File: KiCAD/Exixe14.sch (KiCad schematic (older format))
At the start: 18 parts, among them U4 EXIXE14, U5 EXIXE14, U6 EXIXE14, U7 EXIXE14, U8 EXIXE14, U9 EXIXE14

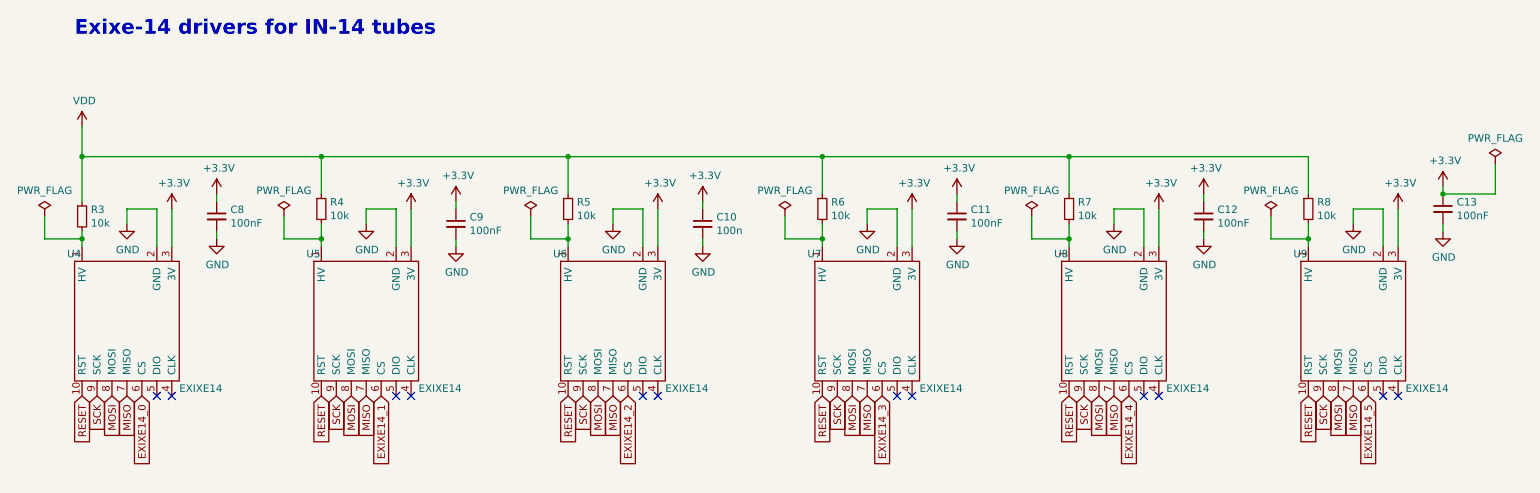
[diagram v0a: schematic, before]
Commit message: v01.2: Updated component numbers, title block, and added transistor library.
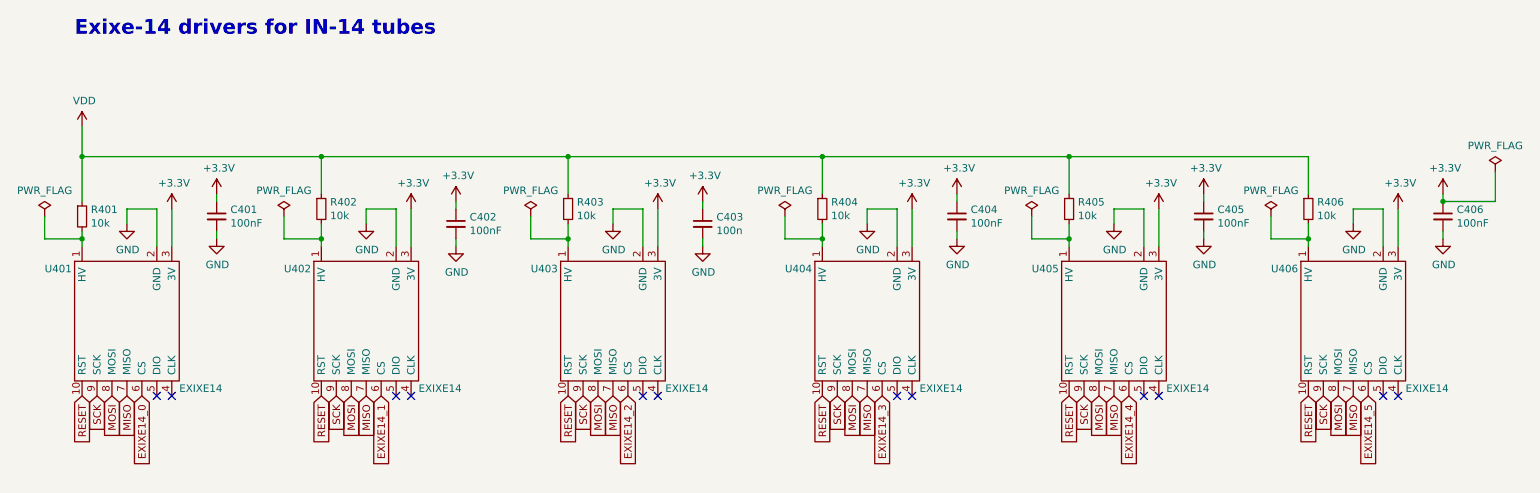
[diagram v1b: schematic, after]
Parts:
- renumbered C8 to C401, C9 to C402, C10 to C403, C11 to C404, C12 to C405, C13 to C406, R3 to R401, R4 to R402, R5 to R403, R6 to R404, R7 to R405, R8 to R406, U4 to U401, U5 to U402, U6 to U403, U7 to U404, U8 to U405, U9 to U406
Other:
- moved on the sheet: C406
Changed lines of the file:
@@
 Sheet 4 5
 Title "Nixie Tube Clock Host Board"
-Date "2021-04-20"
-Rev "v01.1"
+Date "2021-04-26"
+Rev "v01.2"
 Comp "University of Alberta (AlbertaSat)"
-Comment1 "License: CC BY 4.0 (https://creativecommons.org/licenses/by/4.0/)"
-Comment2 "Steven Knudsen (ECE dept., Faculty of Engineering, University of Alberta)."
-Comment3 "This schematic was designed with the assistance of "
-Comment4 "Author: Pundeep Hundal                   Co-author: Sichun Xu"
+Comment1 ""
+Comment2 "License: CC BY 4.0 (https://creativecommons.org/licenses/by/4.0/)"
+Comment3 "Co-author: Sichun Xu"
+Comment4 "Author: Pundeep Hundal"
 $EndDescr
 $Comp
@@
 P 1800 3600
 AR Path="/60980F67" Ref="U?"  Part="1"
-AR Path="/6091CAEB/60980F67" Ref="U4"  Part="1"
-F 0 "U4" H 1400 4050 50  0000 L CNN
+AR Path="/6091CAEB/60980F67" Ref="U401"  Part="1"
+F 0 "U401" H 1250 3950 50  0000 L CNN
 F 1 "EXIXE14" H 2150 3150 50  0000 L CNN
 F 2 "" H 1800 3300 50  0001 C CNN
@@
 P 3400 3600
 AR Path="/60980F6D" Ref="U?"  Part="1"
-AR Path="/6091CAEB/60980F6D" Ref="U5"  Part="1"
-F 0 "U5" H 3000 4050 50  0000 L CNN
+AR Path="/6091CAEB/60980F6D" Ref="U402"  Part="1"
+F 0 "U402" H 2850 3950 50  0000 L CNN
 F 1 "EXIXE14" H 3750 3150 50  0000 L CNN
 F 2 "" H 3400 3300 50  0001 C CNN
@@
 P 5050 3600
 AR Path="/60980F73" Ref="U?"  Part="1"
-AR Path="/6091CAEB/60980F73" Ref="U6"  Part="1"
-F 0 "U6" H 4650 4050 50  0000 L CNN
+AR Path="/6091CAEB/60980F73" Ref="U403"  Part="1"
+F 0 "U403" H 4500 3950 50  0000 L CNN
 F 1 "EXIXE14" H 5400 3150 50  0000 L CNN
 F 2 "" H 5050 3300 50  0001 C CNN
@@
 P 6750 3600
 AR Path="/60980F79" Ref="U?"  Part="1"
-AR Path="/6091CAEB/60980F79" Ref="U7"  Part="1"
-F 0 "U7" H 6350 4050 50  0000 L CNN
+AR Path="/6091CAEB/60980F79" Ref="U404"  Part="1"
+F 0 "U404" H 6200 3950 50  0000 L CNN
 F 1 "EXIXE14" H 7100 3150 50  0000 L CNN
 F 2 "" H 6750 3300 50  0001 C CNN
@@
 P 8400 3600
 AR Path="/60980F7F" Ref="U?"  Part="1"
-AR Path="/6091CAEB/60980F7F" Ref="U8"  Part="1"
-F 0 "U8" H 8000 4050 50  0000 L CNN
+AR Path="/6091CAEB/60980F7F" Ref="U405"  Part="1"
+F 0 "U405" H 7850 3950 50  0000 L CNN
 F 1 "EXIXE14" H 8750 3150 50  0000 L CNN
 F 2 "" H 8400 3300 50  0001 C CNN
@@
 P 10000 3600
 AR Path="/60980F85" Ref="U?"  Part="1"
-AR Path="/6091CAEB/60980F85" Ref="U9"  Part="1"
-F 0 "U9" H 9600 4050 50  0000 L CNN
+AR Path="/6091CAEB/60980F85" Ref="U406"  Part="1"
+F 0 "U406" H 9450 3950 50  0000 L CNN
 F 1 "EXIXE14" H 10350 3150 50  0000 L CNN
 F 2 "" H 10000 3300 50  0001 C CNN
@@
 P 2400 2900
 AR Path="/60981009" Ref="C?"  Part="1"
-AR Path="/6091CAEB/60981009" Ref="C8"  Part="1"
-F 0 "C8" H 2492 2946 50  0000 L CNN
+AR Path="/6091CAEB/60981009" Ref="C401"  Part="1"
+F 0 "C401" H 2492 2946 50  0000 L CNN
 F 1 "100nF" H 2492 2855 50  0000 L CNN
 F 2 "" H 2400 2900 50  0001 C CNN
@@
 P 4000 2950
 AR Path="/60981017" Ref="C?"  Part="1"
-AR Path="/6091CAEB/60981017" Ref="C9"  Part="1"
-F 0 "C9" H 4092 2996 50  0000 L CNN
+AR Path="/6091CAEB/60981017" Ref="C402"  Part="1"
+F 0 "C402" H 4092 2996 50  0000 L CNN
 F 1 "100nF" H 4092 2905 50  0000 L CNN
 F 2 "" H 4000 2950 50  0001 C CNN
@@
 P 5650 2950
 AR Path="/6098101D" Ref="C?"  Part="1"
-AR Path="/6091CAEB/6098101D" Ref="C10"  Part="1"
-F 0 "C10" H 5742 2996 50  0000 L CNN
+AR Path="/6091CAEB/6098101D" Ref="C403"  Part="1"
+F 0 "C403" H 5742 2996 50  0000 L CNN
 F 1 "100n" H 5742 2905 50  0000 L CNN
 F 2 "" H 5650 2950 50  0001 C CNN
@@
 P 7350 2900
 AR Path="/60981023" Ref="C?"  Part="1"
-AR Path="/6091CAEB/60981023" Ref="C11"  Part="1"
-F 0 "C11" H 7442 2946 50  0000 L CNN
+AR Path="/6091CAEB/60981023" Ref="C404"  Part="1"
+F 0 "C404" H 7442 2946 50  0000 L CNN
 F 1 "100nF" H 7442 2855 50  0000 L CNN
 F 2 "" H 7350 2900 50  0001 C CNN
@@
 P 9000 2900
 AR Path="/60981029" Ref="C?"  Part="1"
-AR Path="/6091CAEB/60981029" Ref="C12"  Part="1"
-F 0 "C12" H 9092 2946 50  0000 L CNN
+AR Path="/6091CAEB/60981029" Ref="C405"  Part="1"
+F 0 "C405" H 9092 2946 50  0000 L CNN
 F 1 "100nF" H 9092 2855 50  0000 L CNN
 F 2 "" H 9000 2900 50  0001 C CNN
@@
 L Device:C_Small C?
 U 1 1 6098102F
-P 10600 2850
+P 10600 2900
 AR Path="/6098102F" Ref="C?"  Part="1"
-AR Path="/6091CAEB/6098102F" Ref="C13"  Part="1"
-F 0 "C13" H 10692 2896 50  0000 L CNN
-F 1 "100nF" H 10692 2805 50  0000 L CNN
-F 2 "" H 10600 2850 50  0001 C CNN
-F 3 "~" H 10600 2850 50  0001 C CNN
-	1    10600 2850
+AR Path="/6091CAEB/6098102F" Ref="C406"  Part="1"
+F 0 "C406" H 10692 2946 50  0000 L CNN
+F 1 "100nF" H 10692 2855 50  0000 L CNN
+F 2 "" H 10600 2900 50  0001 C CNN
+F 3 "~" H 10600 2900 50  0001 C CNN
+	1    10600 2900
 	1    0    0    -1
 $EndComp
@@
 L power:+3.3V #PWR?
 U 1 1 6098106D
-P 10600 2700
+P 10600 2750
 AR Path="/6098106D" Ref="#PWR?"  Part="1"
 AR Path="/6091CAEB/6098106D" Ref="#PWR048"  Part="1"
-F 0 "#PWR048" H 10600 2550 50  0001 C CNN
-F 1 "+3.3V" H 10615 2873 50  0000 C CNN
-F 2 "" H 10600 2700 50  0001 C CNN
-F 3 "" H 10600 2700 50  0001 C CNN
-	1    10600 2700
-	1    0    0    -1
-$EndComp
-Wire Wire Line
-	10600 2700 10600 2750
+F 0 "#PWR048" H 10600 2600 50  0001 C CNN
+F 1 "+3.3V" H 10615 2923 50  0000 C CNN
+F 2 "" H 10600 2750 50  0001 C CNN
+F 3 "" H 10600 2750 50  0001 C CNN
+	1    10600 2750
+	1    0    0    -1
+$EndComp
+Wire Wire Line
+	10600 2750 10600 2800
 $Comp
 L power:GND #PWR?
 U 1 1 60981074
-P 10600 3000
+P 10600 3050
 AR Path="/60981074" Ref="#PWR?"  Part="1"
 AR Path="/6091CAEB/60981074" Ref="#PWR049"  Part="1"
-F 0 "#PWR049" H 10600 2750 50  0001 C CNN
-F 1 "GND" H 10605 2827 50  0000 C CNN
-F 2 "" H 10600 3000 50  0001 C CNN
-F 3 "" H 10600 3000 50  0001 C CNN
-	1    10600 3000
-	1    0    0    -1
-$EndComp
-Wire Wire Line
-	10600 3000 10600 2950
+F 0 "#PWR049" H 10600 2800 50  0001 C CNN
+F 1 "GND" H 10605 2877 50  0000 C CNN
+F 2 "" H 10600 3050 50  0001 C CNN
+F 3 "" H 10600 3050 50  0001 C CNN
+	1    10600 3050
+	1    0    0    -1
+$EndComp
+Wire Wire Line
+	10600 3050 10600 3000
 $Comp
 L Device:R_Small R?
@@
 P 3100 2850
 AR Path="/6098107B" Ref="R?"  Part="1"
-AR Path="/6091CAEB/6098107B" Ref="R4"  Part="1"
-F 0 "R4" H 3159 2896 50  0000 L CNN
+AR Path="/6091CAEB/6098107B" Ref="R402"  Part="1"
+F 0 "R402" H 3159 2896 50  0000 L CNN
 F 1 "10k" H 3159 2805 50  0000 L CNN
 F 2 "" H 3100 2850 50  0001 C CNN
@@
 P 4750 2850
 AR Path="/60981082" Ref="R?"  Part="1"
-AR Path="/6091CAEB/60981082" Ref="R5"  Part="1"
-F 0 "R5" H 4809 2896 50  0000 L CNN
+AR Path="/6091CAEB/60981082" Ref="R403"  Part="1"
+F 0 "R403" H 4809 2896 50  0000 L CNN
 F 1 "10k" H 4809 2805 50  0000 L CNN
 F 2 "" H 4750 2850 50  0001 C CNN
@@
 P 8100 2850
 AR Path="/60981089" Ref="R?"  Part="1"
-AR Path="/6091CAEB/60981089" Ref="R7"  Part="1"
-F 0 "R7" H 8159 2896 50  0000 L CNN
+AR Path="/6091CAEB/60981089" Ref="R405"  Part="1"
+F 0 "R405" H 8159 2896 50  0000 L CNN
 F 1 "10k" H 8159 2805 50  0000 L CNN
 F 2 "" H 8100 2850 50  0001 C CNN
@@
 P 1500 2900
 AR Path="/60981090" Ref="R?"  Part="1"
-AR Path="/6091CAEB/60981090" Ref="R3"  Part="1"
-F 0 "R3" H 1559 2946 50  0000 L CNN
+AR Path="/6091CAEB/60981090" Ref="R401"  Part="1"
+F 0 "R401" H 1559 2946 50  0000 L CNN
 F 1 "10k" H 1559 2855 50  0000 L CNN
 F 2 "" H 1500 2900 50  0001 C CNN
@@
 P 9700 2850
 AR Path="/60981096" Ref="R?"  Part="1"
-AR Path="/6091CAEB/60981096" Ref="R8"  Part="1"
-F 0 "R8" H 9759 2896 50  0000 L CNN
+AR Path="/6091CAEB/60981096" Ref="R406"  Part="1"
+F 0 "R406" H 9759 2896 50  0000 L CNN
 F 1 "10k" H 9759 2805 50  0000 L CNN
 F 2 "" H 9700 2850 50  0001 C CNN
@@
 P 6450 2850
 AR Path="/6098109C" Ref="R?"  Part="1"
-AR Path="/6091CAEB/6098109C" Ref="R6"  Part="1"
-F 0 "R6" H 6509 2896 50  0000 L CNN
+AR Path="/6091CAEB/6098109C" Ref="R404"  Part="1"
+F 0 "R404" H 6509 2896 50  0000 L CNN
 F 1 "10k" H 6509 2805 50  0000 L CNN
 F 2 "" H 6450 2850 50  0001 C CNN
@@
 L power:PWR_FLAG #FLG0103
 U 1 1 60A6FB0C
-P 10950 2550
-F 0 "#FLG0103" H 10950 2625 50  0001 C CNN
-F 1 "PWR_FLAG" H 10950 2723 50  0000 C CNN
-F 2 "" H 10950 2550 50  0001 C CNN
-F 3 "~" H 10950 2550 50  0001 C CNN
-	1    10950 2550
-	1    0    0    -1
-$EndComp
-Wire Wire Line
-	10950 2550 10950 2750
-Wire Wire Line
-	10950 2750 10600 2750
-Connection ~ 10600 2750
+P 10950 2600
+F 0 "#FLG0103" H 10950 2675 50  0001 C CNN
+F 1 "PWR_FLAG" H 10950 2773 50  0000 C CNN
+F 2 "" H 10950 2600 50  0001 C CNN
+F 3 "~" H 10950 2600 50  0001 C CNN
+	1    10950 2600
+	1    0    0    -1
+$EndComp
+Wire Wire Line
+	10950 2600 10950 2800
+Wire Wire Line
+	10950 2800 10600 2800
+Connection ~ 10600 2800
 $EndSCHEMATC
